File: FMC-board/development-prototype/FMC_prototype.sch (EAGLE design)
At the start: 65 parts, among them J1 DC_POWER_JACK-PJ-102AH, J2 DC_POWER_JACK-PJ-102AH

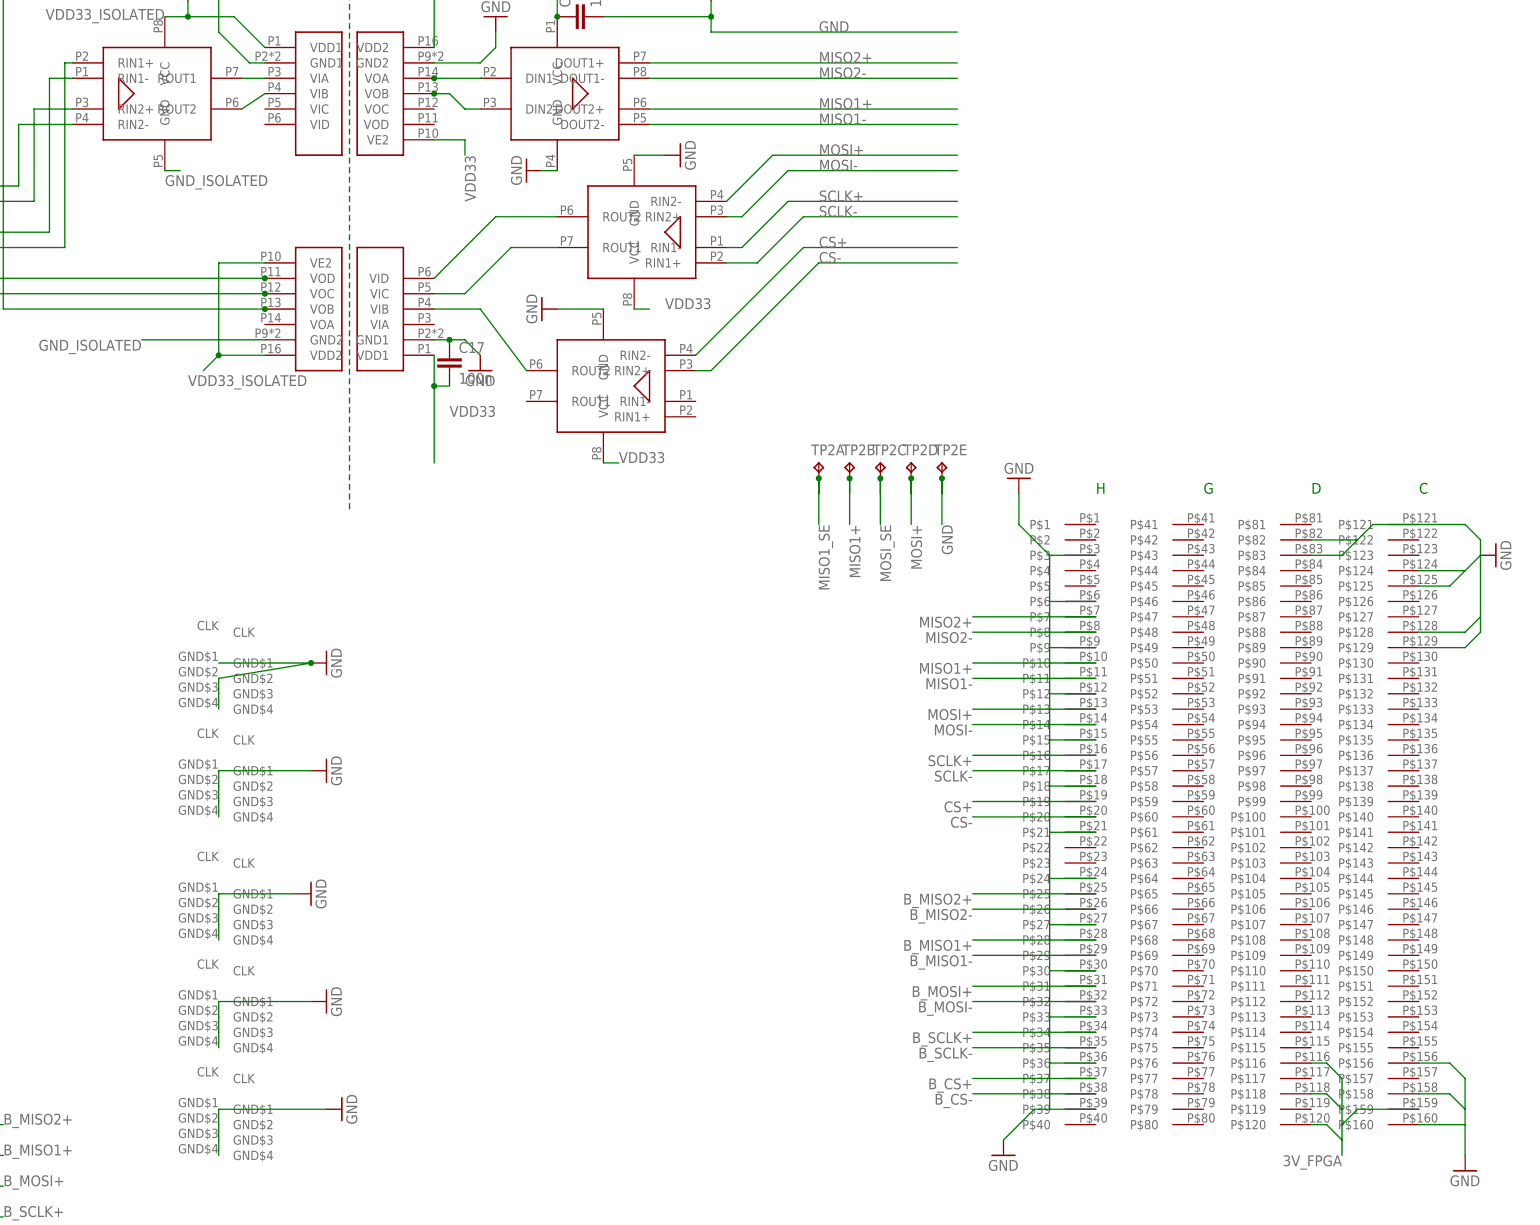
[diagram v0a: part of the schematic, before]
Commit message: added testpoints
still some unrouted parts
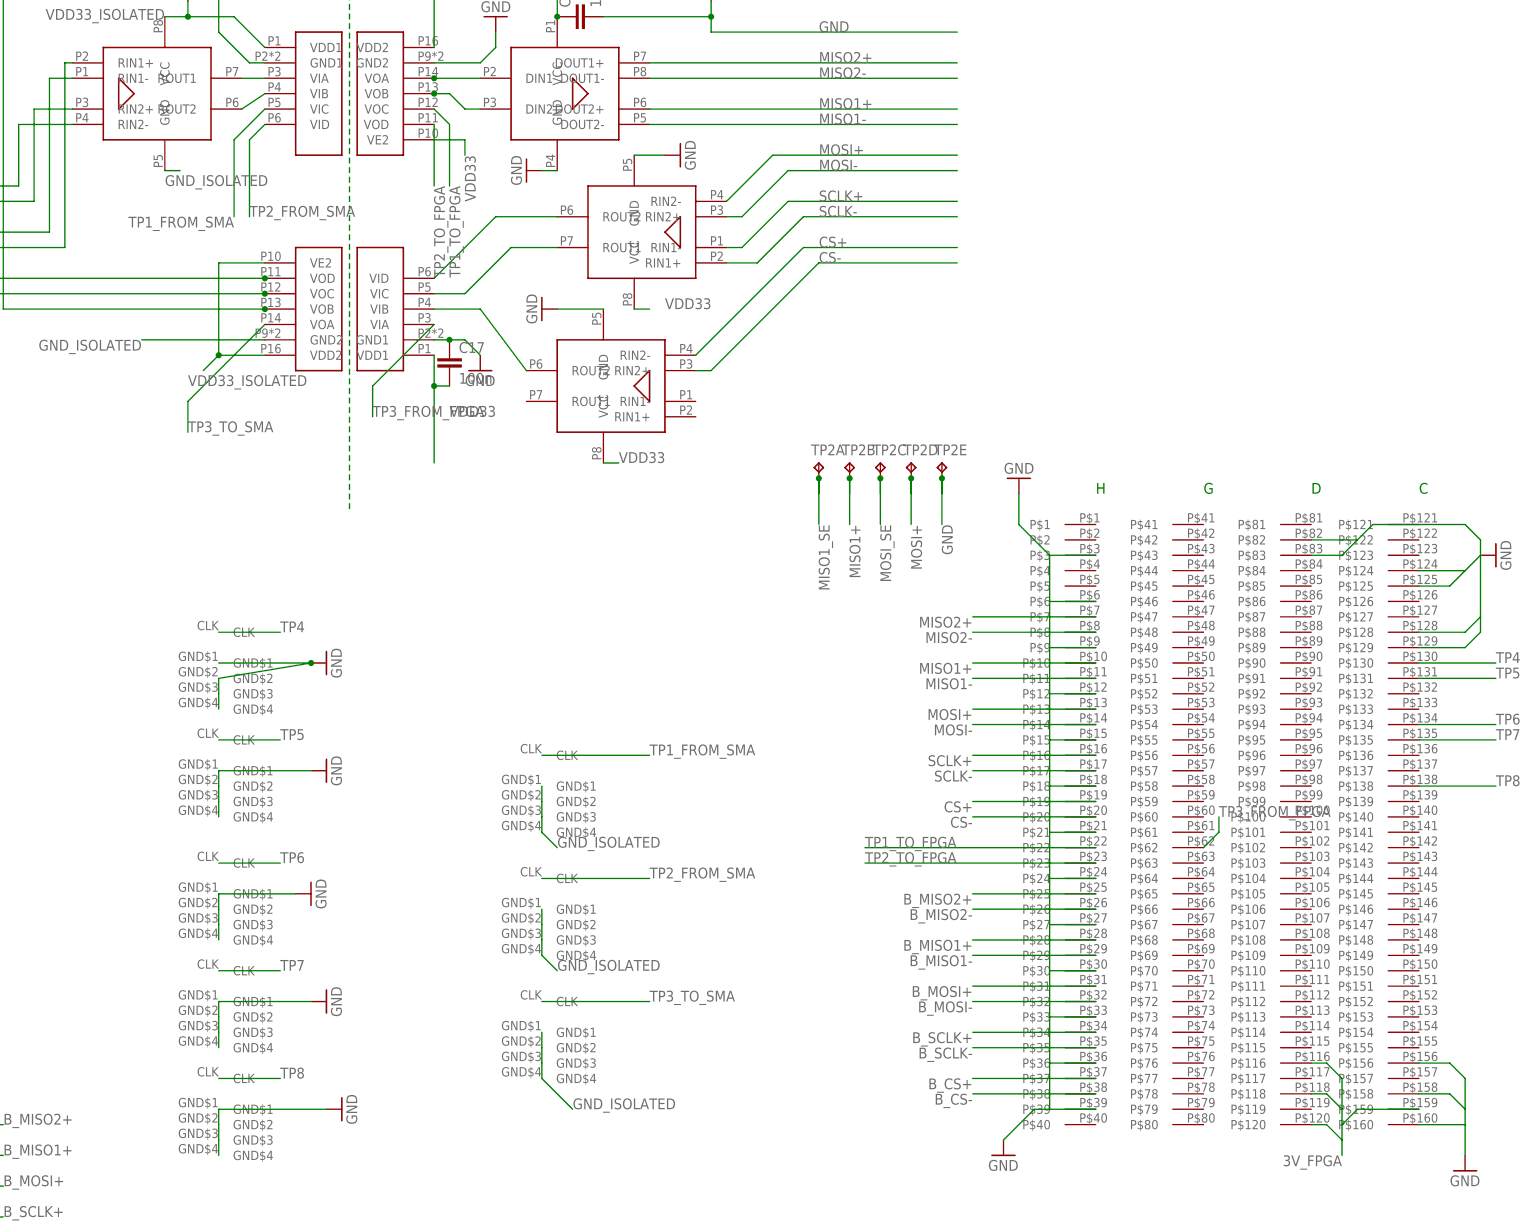
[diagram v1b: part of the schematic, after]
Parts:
- added U$17, U$18, U$19: SMA_JACK_142-0701-201_DEV, SA_BB:SMA_JACK_142-0701-201_DEV
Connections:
- new net TP1_FROM_SMA: U$11.VIC, U$19.CLK
- new net TP1_TO_FPGA: U$11.VOC, U$4G$1.P$22
- new net TP2_FROM_SMA: U$11.VID, U$17.CLK
- new net TP2_TO_FPGA: U$11.VOD, U$4G$1.P$23
- new net TP3_FROM_FPGA: U$12.VIA, U$4G$1.P$62
- new net TP3_TO_SMA: U$12.VOA, U$18.CLK
- new net TP4: U$4G$1.P$130, U$5.CLK
- new net TP5: U$2.CLK, U$4G$1.P$131
- new net TP6: U$13.CLK, U$4G$1.P$134
- new net TP7: U$14.CLK, U$4G$1.P$135
- new net TP8: U$15.CLK, U$4G$1.P$138
- net GND_ISOLATED: now also U$17.GND$1, U$17.GND$2, U$17.GND$3, U$17.GND$4, U$18.GND$1, U$18.GND$2, U$18.GND$3, U$18.GND$4, U$19.GND$1, U$19.GND$2, U$19.GND$3, U$19.GND$4
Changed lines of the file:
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@@
 <?xml version="1.0" encoding="utf-8"?>
 <!DOCTYPE eagle SYSTEM "eagle.dtd">
-<eagle version="7.5.0">
+<eagle version="6.6.0">
 <drawing>
 <settings>
@@
 <part name="GND22" library="supply1" deviceset="GND" device=""/>
 <part name="TP5" library="testpad" deviceset="TP5" device="P5-25-13"/>
+<part name="U$17" library="SA_BB" deviceset="SMA_JACK_142-0701-201_DEV" device=""/>
+<part name="U$18" library="SA_BB" deviceset="SMA_JACK_142-0701-201_DEV" device=""/>
+<part name="U$19" library="SA_BB" deviceset="SMA_JACK_142-0701-201_DEV" device=""/>
 </parts>
 <sheets>
@@
 <instance part="TP5" gate="D" x="101.6" y="30.48" rot="R270"/>
 <instance part="TP5" gate="E" x="101.6" y="25.4" rot="R270"/>
+<instance part="U$17" gate="G$1" x="228.6" y="68.58"/>
+<instance part="U$18" gate="G$1" x="228.6" y="48.26"/>
+<instance part="U$19" gate="G$1" x="228.6" y="88.9"/>
 </instances>
 <busses>
@@
 <label x="45.72" y="350.52" size="1.778" layer="95" rot="R270"/>
 </segment>
+<segment>
+<pinref part="U$17" gate="G$1" pin="GND$1"/>
+<pinref part="U$17" gate="G$1" pin="GND$2"/>
+<wire x1="195.58" y1="81.28" x2="195.58" y2="78.74" width="0.1524" layer="91"/>
+<pinref part="U$17" gate="G$1" pin="GND$3"/>
+<wire x1="195.58" y1="78.74" x2="195.58" y2="76.2" width="0.1524" layer="91"/>
+<pinref part="U$17" gate="G$1" pin="GND$4"/>
+<wire x1="195.58" y1="76.2" x2="195.58" y2="73.66" width="0.1524" layer="91"/>
+<wire x1="195.58" y1="73.66" x2="198.12" y2="71.12" width="0.1524" layer="91"/>
+<label x="198.12" y="71.12" size="1.778" layer="95"/>
+</segment>
+<segment>
+<pinref part="U$18" gate="G$1" pin="GND$1"/>
+<pinref part="U$18" gate="G$1" pin="GND$2"/>
+<wire x1="195.58" y1="60.96" x2="195.58" y2="58.42" width="0.1524" layer="91"/>
+<pinref part="U$18" gate="G$1" pin="GND$3"/>
+<wire x1="195.58" y1="58.42" x2="195.58" y2="55.88" width="0.1524" layer="91"/>
+<pinref part="U$18" gate="G$1" pin="GND$4"/>
+<wire x1="195.58" y1="55.88" x2="195.58" y2="53.34" width="0.1524" layer="91"/>
+<wire x1="195.58" y1="53.34" x2="200.66" y2="48.26" width="0.1524" layer="91"/>
+<label x="200.66" y="48.26" size="1.778" layer="95"/>
+</segment>
+<segment>
+<pinref part="U$19" gate="G$1" pin="GND$1"/>
+<pinref part="U$19" gate="G$1" pin="GND$2"/>
+<wire x1="195.58" y1="101.6" x2="195.58" y2="99.06" width="0.1524" layer="91"/>
+<pinref part="U$19" gate="G$1" pin="GND$3"/>
+<wire x1="195.58" y1="99.06" x2="195.58" y2="96.52" width="0.1524" layer="91"/>
+<pinref part="U$19" gate="G$1" pin="GND$4"/>
+<wire x1="195.58" y1="96.52" x2="195.58" y2="93.98" width="0.1524" layer="91"/>
+<wire x1="195.58" y1="93.98" x2="198.12" y2="91.44" width="0.1524" layer="91"/>
+<label x="198.12" y="91.44" size="1.778" layer="95"/>
+</segment>
 </net>
 <net name="VDD_ISOLATED" class="0">
@@
 </segment>
 </net>
+<net name="TP1_FROM_SMA" class="0">
+<segment>
+<pinref part="U$11" gate="G$1" pin="VIC"/>
+<wire x1="149.86" y1="213.36" x2="144.78" y2="208.28" width="0.1524" layer="91"/>
+<wire x1="144.78" y1="208.28" x2="144.78" y2="195.58" width="0.1524" layer="91"/>
+<label x="144.78" y="195.58" size="1.778" layer="95" rot="R180"/>
+</segment>
+<segment>
+<pinref part="U$19" gate="G$1" pin="CLK"/>
+<wire x1="195.58" y1="106.68" x2="213.36" y2="106.68" width="0.1524" layer="91"/>
+<label x="213.36" y="106.68" size="1.778" layer="95"/>
+</segment>
+</net>
+<net name="TP2_FROM_SMA" class="0">
+<segment>
+<pinref part="U$11" gate="G$1" pin="VID"/>
+<wire x1="149.86" y1="210.82" x2="147.32" y2="208.28" width="0.1524" layer="91"/>
+<wire x1="147.32" y1="208.28" x2="147.32" y2="195.58" width="0.1524" layer="91"/>
+<label x="147.32" y="195.58" size="1.778" layer="95"/>
+</segment>
+<segment>
+<pinref part="U$17" gate="G$1" pin="CLK"/>
+<wire x1="195.58" y1="86.36" x2="213.36" y2="86.36" width="0.1524" layer="91"/>
+<label x="213.36" y="86.36" size="1.778" layer="95"/>
+</segment>
+</net>
+<net name="TP1_TO_FPGA" class="0">
+<segment>
+<pinref part="U$11" gate="G$1" pin="VOC"/>
+<wire x1="177.8" y1="213.36" x2="180.34" y2="210.82" width="0.1524" layer="91"/>
+<wire x1="180.34" y1="210.82" x2="180.34" y2="200.66" width="0.1524" layer="91"/>
+<label x="180.34" y="200.66" size="1.778" layer="95" rot="R270"/>
+</segment>
+<segment>
+<pinref part="U$4" gate="G$1" pin="P$22"/>
+<wire x1="287.02" y1="91.44" x2="248.92" y2="91.44" width="0.1524" layer="91"/>
+<label x="248.92" y="91.44" size="1.778" layer="95"/>
+</segment>
+</net>
+<net name="TP2_TO_FPGA" class="0">
+<segment>
+<pinref part="U$11" gate="G$1" pin="VOD"/>
+<wire x1="177.8" y1="210.82" x2="177.8" y2="200.66" width="0.1524" layer="91"/>
+<label x="177.8" y="200.66" size="1.778" layer="95" rot="R270"/>
+</segment>
+<segment>
+<pinref part="U$4" gate="G$1" pin="P$23"/>
+<wire x1="287.02" y1="88.9" x2="248.92" y2="88.9" width="0.1524" layer="91"/>
+<label x="248.92" y="88.9" size="1.778" layer="95"/>
+</segment>
+</net>
+<net name="TP3_TO_SMA" class="0">
+<segment>
+<pinref part="U$18" gate="G$1" pin="CLK"/>
+<wire x1="195.58" y1="66.04" x2="213.36" y2="66.04" width="0.1524" layer="91"/>
+<label x="213.36" y="66.04" size="1.778" layer="95"/>
+</segment>
+<segment>
+<pinref part="U$12" gate="G$1" pin="VOA"/>
+<wire x1="149.86" y1="177.8" x2="137.16" y2="165.1" width="0.1524" layer="91"/>
+<wire x1="137.16" y1="165.1" x2="137.16" y2="160.02" width="0.1524" layer="91"/>
+<label x="137.16" y="160.02" size="1.778" layer="95"/>
+</segment>
+</net>
+<net name="TP3_FROM_FPGA" class="0">
+<segment>
+<pinref part="U$12" gate="G$1" pin="VIA"/>
+<wire x1="177.8" y1="177.8" x2="167.64" y2="167.64" width="0.1524" layer="91"/>
+<wire x1="167.64" y1="167.64" x2="167.64" y2="162.56" width="0.1524" layer="91"/>
+<label x="167.64" y="162.56" size="1.778" layer="95"/>
+</segment>
+<segment>
+<pinref part="U$4" gate="G$1" pin="P$62"/>
+<wire x1="304.8" y1="91.44" x2="307.34" y2="93.98" width="0.1524" layer="91"/>
+<wire x1="307.34" y1="93.98" x2="307.34" y2="96.52" width="0.1524" layer="91"/>
+<label x="307.34" y="96.52" size="1.778" layer="95"/>
+</segment>
+</net>
+<net name="TP4" class="0">
+<segment>
+<pinref part="U$4" gate="G$1" pin="P$130"/>
+<wire x1="340.36" y1="121.92" x2="353.06" y2="121.92" width="0.1524" layer="91"/>
+<label x="353.06" y="121.92" size="1.778" layer="95"/>
+</segment>
+<segment>
+<pinref part="U$5" gate="G$1" pin="CLK"/>
+<wire x1="142.24" y1="127" x2="152.4" y2="127" width="0.1524" layer="91"/>
+<label x="152.4" y="127" size="1.778" layer="95"/>
+</segment>
+</net>
+<net name="TP5" class="0">
+<segment>
+<pinref part="U$4" gate="G$1" pin="P$131"/>
+<wire x1="340.36" y1="119.38" x2="353.06" y2="119.38" width="0.1524" layer="91"/>
+<label x="353.06" y="119.38" size="1.778" layer="95"/>
+</segment>
+<segment>
+<pinref part="U$2" gate="G$1" pin="CLK"/>
+<wire x1="142.24" y1="109.22" x2="152.4" y2="109.22" width="0.1524" layer="91"/>
+<label x="152.4" y="109.22" size="1.778" layer="95"/>
+</segment>
+</net>
+<net name="TP6" class="0">
+<segment>
+<pinref part="U$4" gate="G$1" pin="P$134"/>
+<wire x1="340.36" y1="111.76" x2="353.06" y2="111.76" width="0.1524" layer="91"/>
+<label x="353.06" y="111.76" size="1.778" layer="95"/>
+</segment>
+<segment>
+<pinref part="U$13" gate="G$1" pin="CLK"/>
+<wire x1="142.24" y1="88.9" x2="152.4" y2="88.9" width="0.1524" layer="91"/>
+<label x="152.4" y="88.9" size="1.778" layer="95"/>
+</segment>
+</net>
+<net name="TP7" class="0">
+<segment>
+<pinref part="U$4" gate="G$1" pin="P$135"/>
+<wire x1="340.36" y1="109.22" x2="353.06" y2="109.22" width="0.1524" layer="91"/>
+<label x="353.06" y="109.22" size="1.778" layer="95"/>
+</segment>
+<segment>
+<pinref part="U$14" gate="G$1" pin="CLK"/>
+<wire x1="142.24" y1="71.12" x2="152.4" y2="71.12" width="0.1524" layer="91"/>
+<label x="152.4" y="71.12" size="1.778" layer="95"/>
+</segment>
+</net>
+<net name="TP8" class="0">
+<segment>
+<pinref part="U$4" gate="G$1" pin="P$138"/>
+<wire x1="340.36" y1="101.6" x2="353.06" y2="101.6" width="0.1524" layer="91"/>
+<label x="353.06" y="101.6" size="1.778" layer="95"/>
+</segment>
+<segment>
+<pinref part="U$15" gate="G$1" pin="CLK"/>
+<wire x1="142.24" y1="53.34" x2="152.4" y2="53.34" width="0.1524" layer="91"/>
+<label x="152.4" y="53.34" size="1.778" layer="95"/>
+</segment>
+</net>
